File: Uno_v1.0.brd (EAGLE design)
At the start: 68.6 x 53.3 mm, 62 parts, among them CN1 POWER_JACK, CN2 47346-0001, CN3 DIGITAL10, CN4 DIGITAL8, CN5 ICSP, CN6 POWER8, CN7 ANALOG6, IC1 AMS1117-5.0, IC2 AMS1117-3.3, IC3 MCP6002T-I/SN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

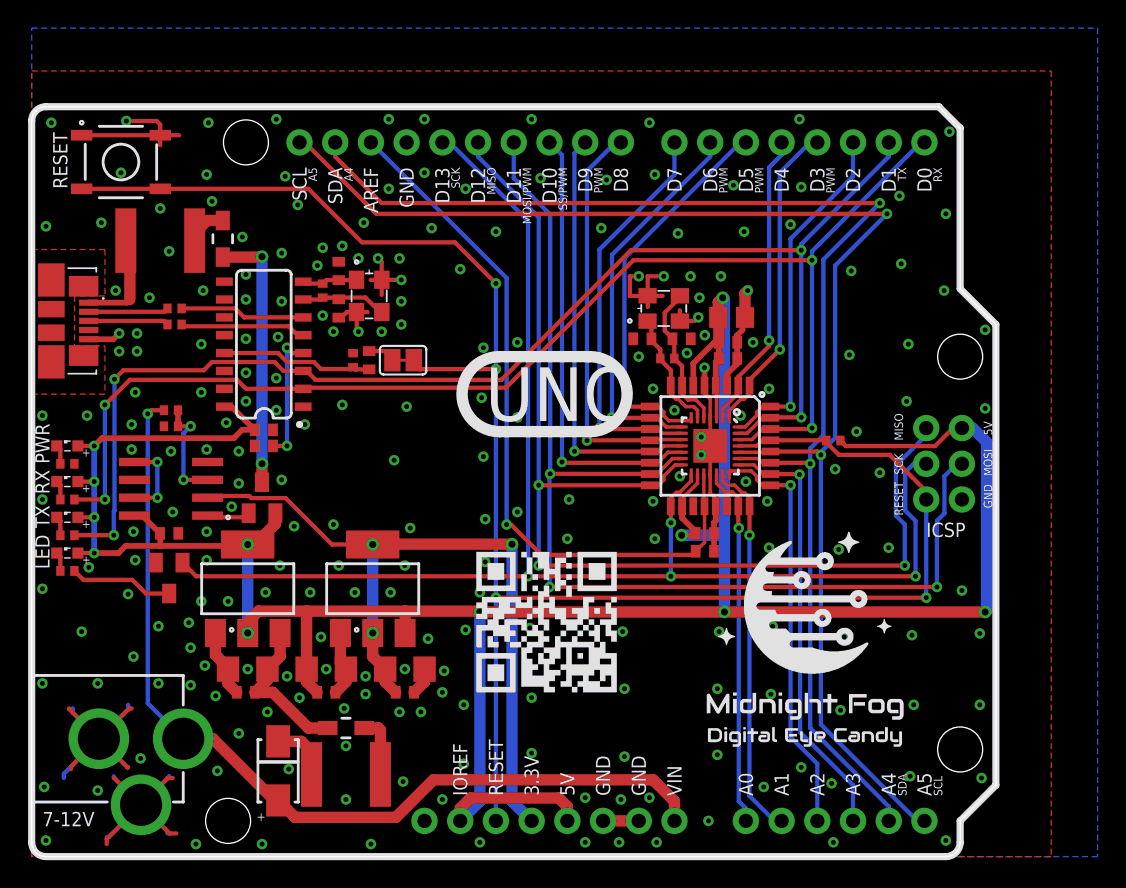
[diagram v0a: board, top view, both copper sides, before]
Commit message: Moved main MCU a little bit to the right. Generated new CAM. Generated new preview.
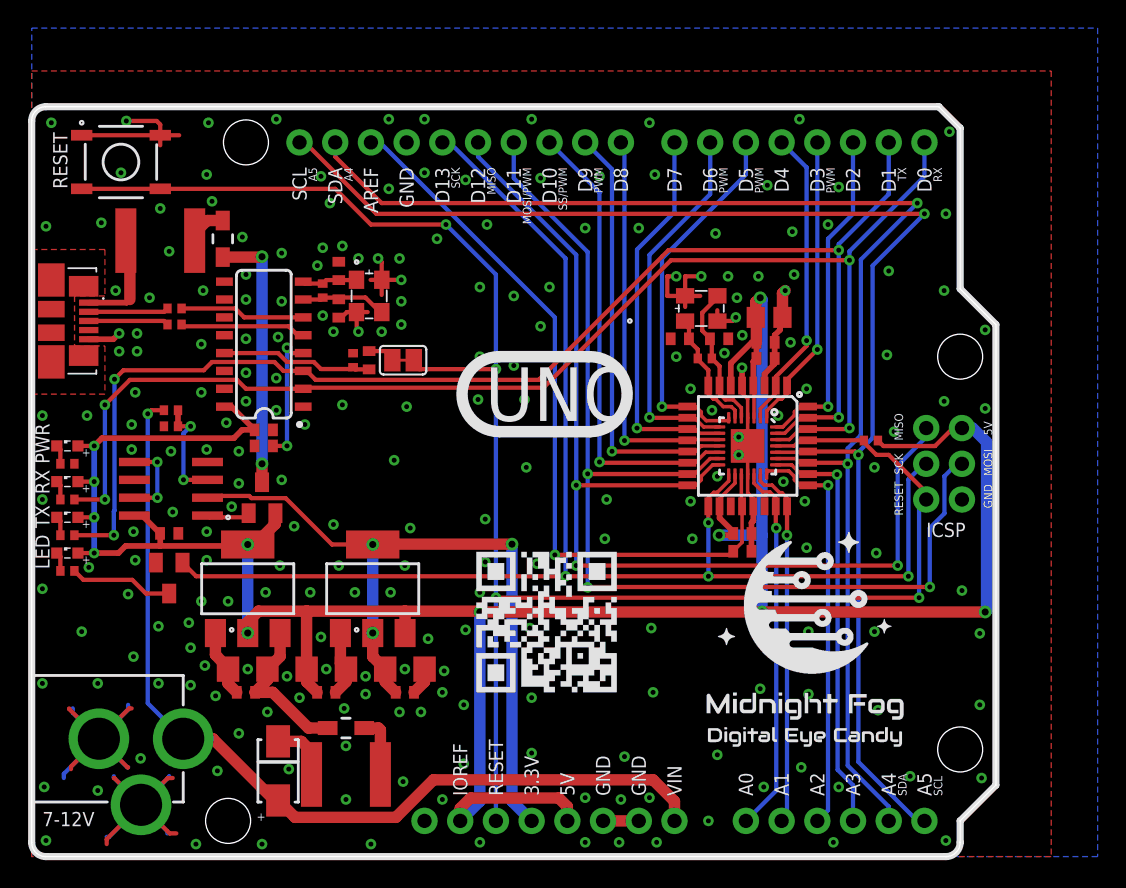
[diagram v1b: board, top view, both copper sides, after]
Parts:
- moved C12 2.67 mm to (48.9, 36.8)
- moved C13 2.67 mm to (46.1, 36.8)
- moved C14 2.67 mm to (52.2, 36.6)
- moved C15 2.67 mm to (52.2, 35.4)
- moved C16 2.67 mm to (50.5, 23.0)
- moved C17 2.67 mm to (52.5, 38.4)
- moved C19 2.67 mm to (50.5, 21.7)
- moved Q2 2.67 mm to (47.6, 39.0)
- moved U2 2.67 mm to (50.9, 29.2)
- moved U3 2.67 mm to (50.9, 29.2)
- moved R12 2.67 mm to (59.7, 29.6)
- moved R6 2.67 mm to (47.9, 35.4)
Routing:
- net 5V: track 205.8 -> 203.1 mm
- net RESET: track 131.1 -> 128.4 mm
- net D12_MISO: track 79.8 -> 77.4 mm
- net AREF: track 51.4 -> 53.7 mm
- net D11_MOSI: track 79.8 -> 78.0 mm
- net D1_TX: track 94.7 -> 96.3 mm
- net A5_SCL: track 98.4 -> 99.9 mm
- net A4_SDA: track 94.7 -> 96.3 mm
- net D0_RX: track 93.3 -> 94.8 mm
- net D3_PWM: track 22.6 -> 21.2 mm
- net D5_PWM: track 28.1 -> 26.8 mm
- net D8: track 29.2 -> 28.1 mm
- net D2: track 25.1 -> 24.0 mm
- net A3: track 30.8 -> 29.7 mm
- net D6_PWM: track 27.7 -> 26.6 mm
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
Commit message: Moved some wires. Generated new CAM. Generated new preview.
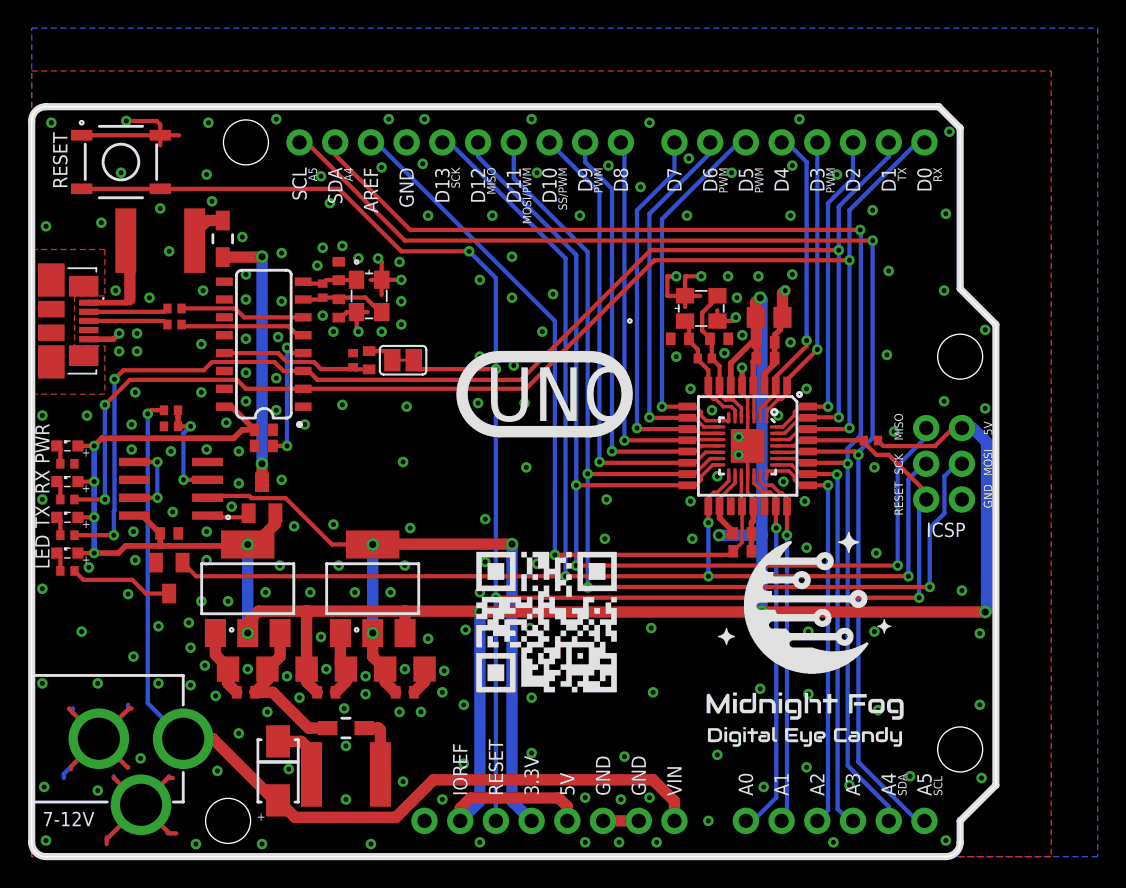
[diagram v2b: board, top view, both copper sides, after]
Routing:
- net A4_SDA: track 96.3 -> 89.4 mm
- net A5_SCL: track 99.9 -> 93.6 mm
- net GND: vias 228 -> 229

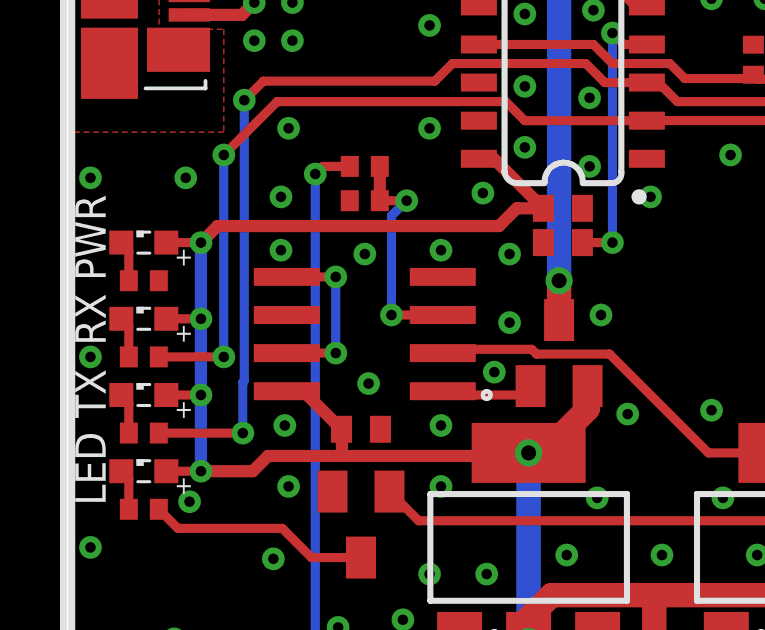
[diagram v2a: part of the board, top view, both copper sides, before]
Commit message: Use LM358D OpAmp instead. Generated new CAM. Generated new PNG preview. Generated new PDF schematic.
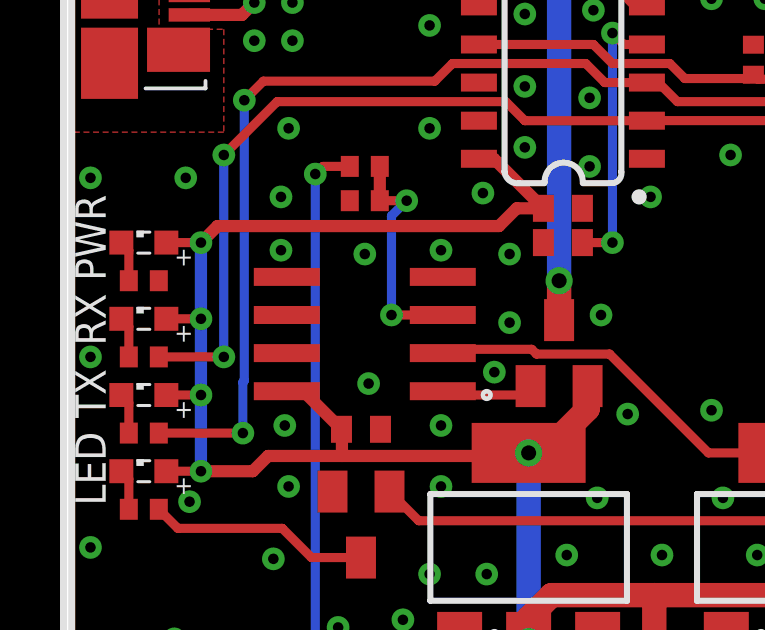
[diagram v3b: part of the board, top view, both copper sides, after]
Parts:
- IC3: value MCP6002T-I/SN -> LM358D
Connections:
- removed net N$1: IC3.5, IC3.7
- net GND: now also IC3.5
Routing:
- net N$1: track 5.81 -> 0.00 mm, vias 2 -> 0
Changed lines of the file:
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@@
 <drawing>
 <settings>
-<setting alwaysvectorfont="yes"/>
+<setting alwaysvectorfont="no"/>
 <setting verticaltext="up"/>
 </settings>
@@
 <attribute name="VALUE" x="22.733" y="42.291" size="0.6096" layer="27" font="vector"/>
 </element>
-<element name="IC3" library="linear" library_urn="urn:adsk.eagle:library:262" package="SO08" package3d_urn="urn:adsk.eagle:package:16404/2" value="MCP6002T-I/SN" x="9.906" y="26.162" smashed="yes" rot="R90">
+<element name="IC3" library="linear" library_urn="urn:adsk.eagle:library:262" package="SO08" package3d_urn="urn:adsk.eagle:package:16404/2" value="LM358D" x="9.906" y="26.162" smashed="yes" rot="R90">
 <attribute name="NAME" x="8.509" y="27.559" size="0.6096" layer="27" font="vector"/>
 <attribute name="POPULARITY" value="4" x="9.906" y="26.162" size="1.778" layer="27" rot="R90" display="off"/>
@@
 <via x="38.989" y="45.593" extent="1-16" drill="0.35"/>
 <via x="35.941" y="48.641" extent="1-16" drill="0.35"/>
+<contactref element="IC3" pad="5"/>
 </signal>
 <signal name="VIN" class="3">
@@
 <wire x1="11.303" y1="30.607" x2="10.406" y2="30.607" width="0.3048" layer="1"/>
 </signal>
-<signal name="N$1">
-<contactref element="IC3" pad="5"/>
-<contactref element="IC3" pad="7"/>
-<wire x1="7.306" y1="25.527" x2="8.9408" y2="25.527" width="0.3048" layer="1"/>
-<via x="8.9408" y="25.527" extent="1-16" drill="0.35"/>
-<via x="8.938" y="28.067" extent="1-16" drill="0.35"/>
-<wire x1="8.938" y1="28.067" x2="8.938" y2="25.5298" width="0.3048" layer="16"/>
-<wire x1="8.9408" y1="25.527" x2="8.938" y2="25.5298" width="0.3048" layer="16"/>
-<wire x1="8.938" y1="28.067" x2="7.306" y2="28.067" width="0.3048" layer="1"/>
-</signal>
 <signal name="MCU_OSC_IN">

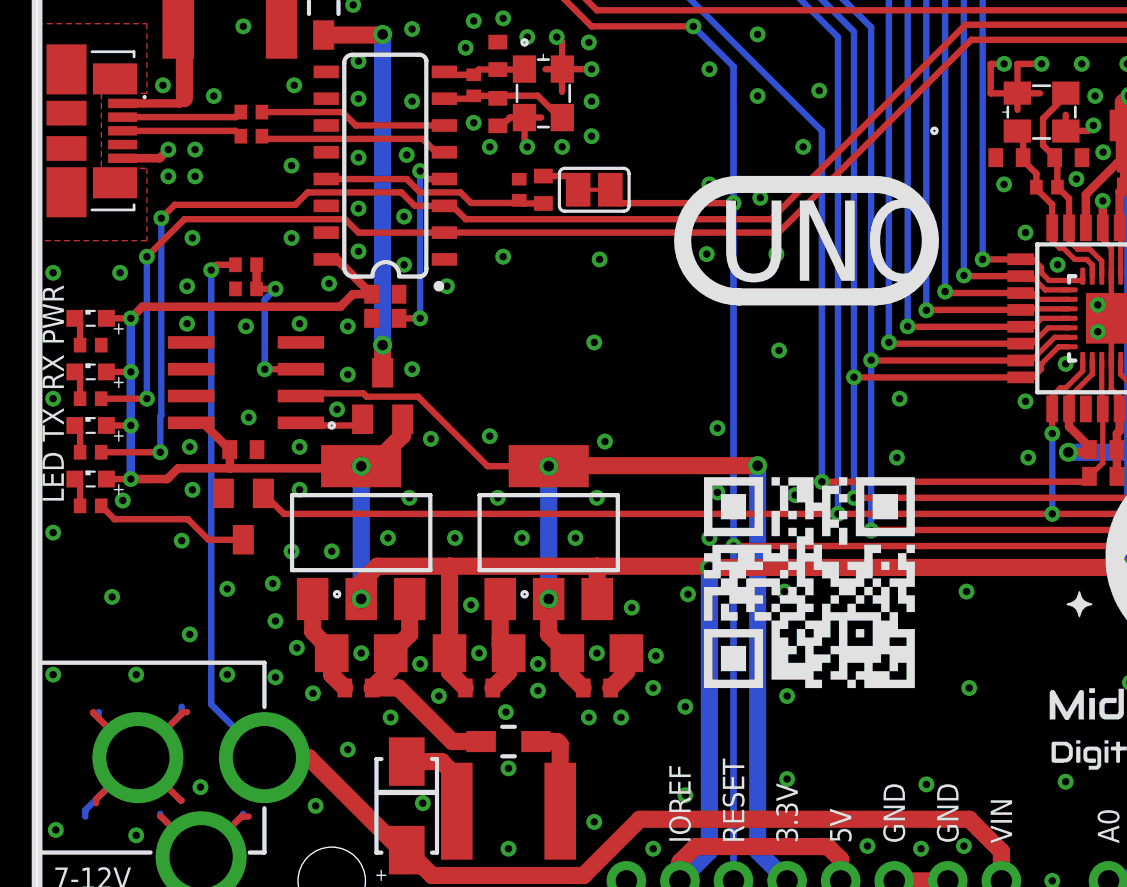
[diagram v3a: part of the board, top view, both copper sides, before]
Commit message: Properly disabled second channel of op amp. Generated new CAM files. Generated new PNG preview. Generated new PDF schematics. Generated new BoM and PnP files.
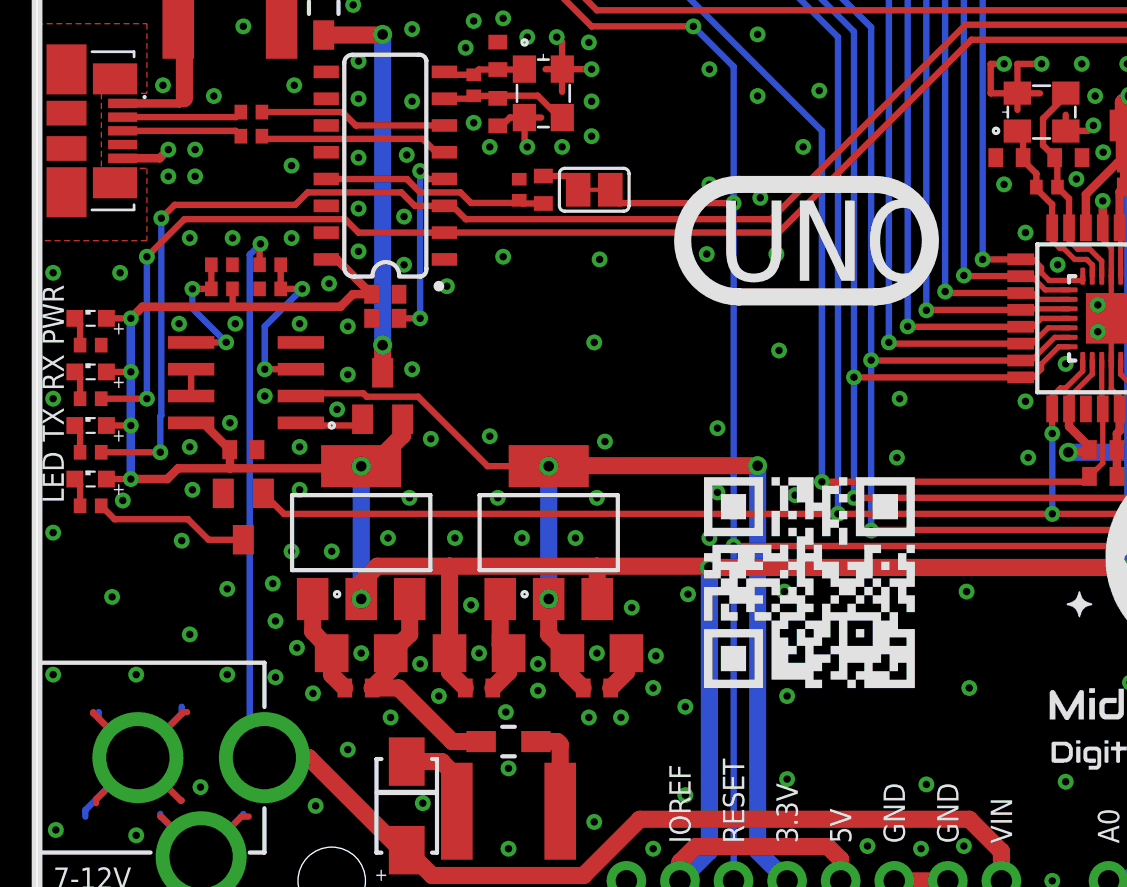
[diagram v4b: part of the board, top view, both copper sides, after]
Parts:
- added R13, R14: 100K, rcl:R0402
- moved R4 1.14 mm to (11.0, 31.8)
- moved R5 1.14 mm to (11.0, 30.6)
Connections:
- new net N$1: IC3.5, R13.1, R14.2
- new net N$15: IC3.6, IC3.7
- net 5V: now also R13.2
- net GND: now also R14.1; no longer IC3.5, IC3.6
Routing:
- net N$1: track 0.00 -> 6.90 mm, vias 0 -> 2
- net N$15: track 0.00 -> 1.27 mm
- net 5V: track 203.1 -> 204.0 mm
- net N$12: track 7.77 -> 8.42 mm
- net GND: vias 229 -> 230

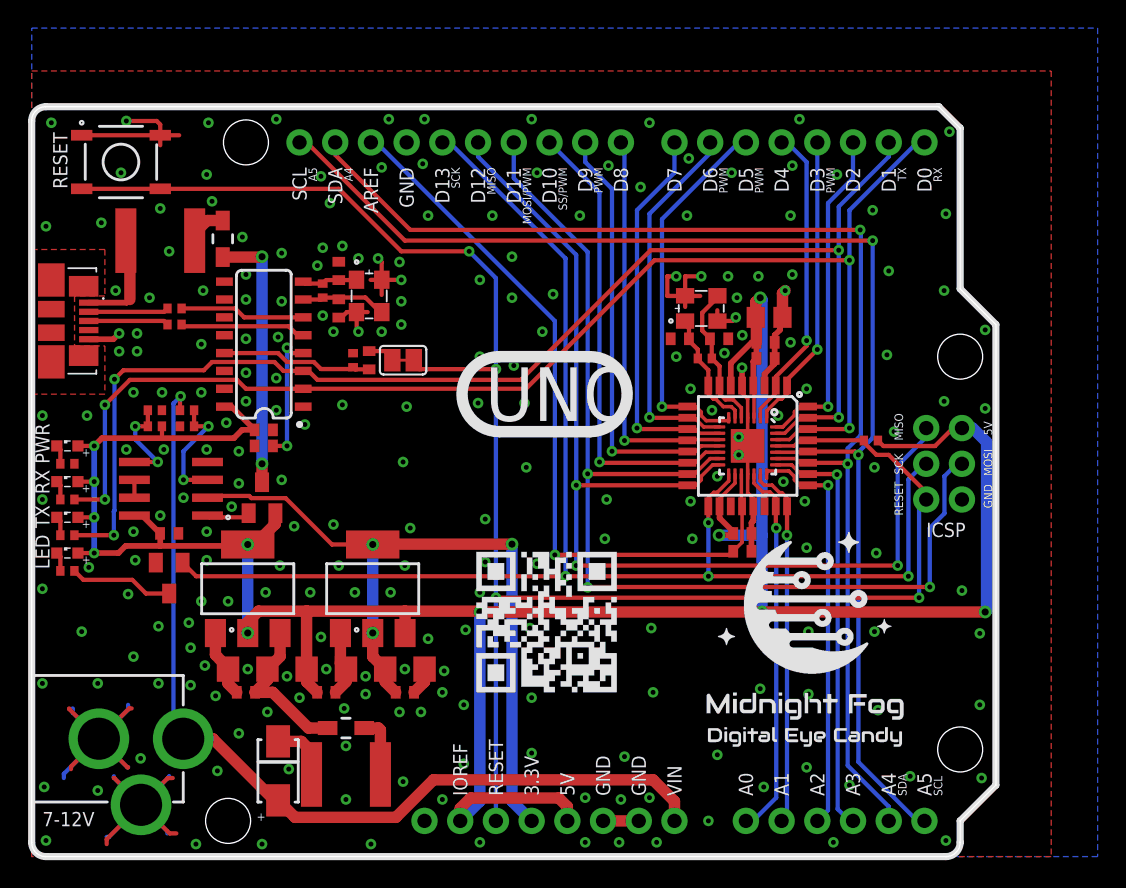
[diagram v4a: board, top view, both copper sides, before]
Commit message: Redone chip wiring for better reverse currents.
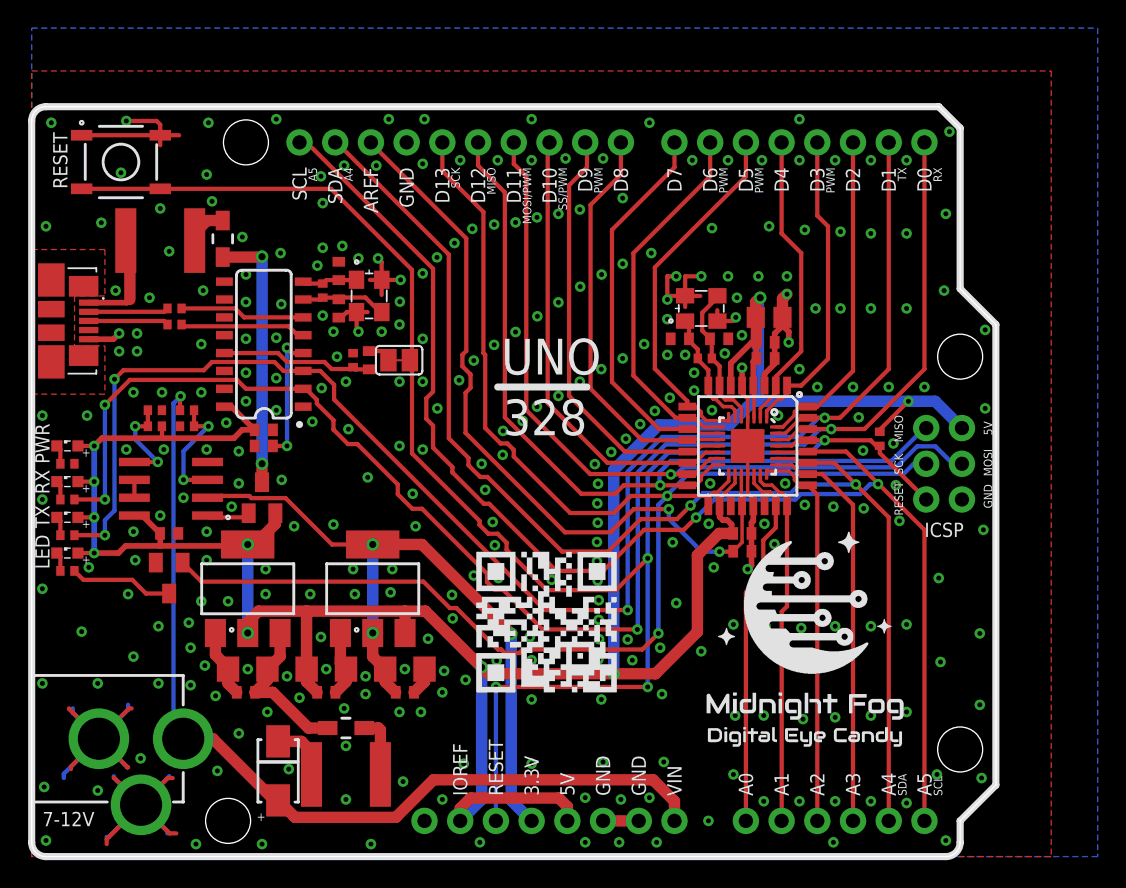
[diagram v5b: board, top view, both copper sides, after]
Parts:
- moved R12 0.65 mm to (60.3, 29.7), turned to 90 degrees
- moved SJ1 0.28 mm to (26.1, 35.3)
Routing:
- net D11_MOSI: track 77.9 -> 57.6 mm, vias 3 -> 1
- net D12_MISO: track 77.4 -> 60.1 mm, vias 3 -> 1
- net D0_RX: track 95.0 -> 111.2 mm
- net D1_TX: track 96.3 -> 110.0 mm
- net D13_SCK: track 103.5 -> 111.1 mm, vias 4 -> 2
- net 5V: track 204.0 -> 196.7 mm, vias 11 -> 10
- net 3.3V: track 55.4 -> 50.8 mm
- net A5_SCL: track 93.6 -> 98.1 mm
- net RESET: track 128.3 -> 124.4 mm
- net GND: track 115.2 -> 118.3 mm, vias 230 -> 313
- net A2: track 29.3 -> 27.8 mm, vias 1 -> 0
- net D3_PWM: track 21.2 -> 22.4 mm, vias 1 -> 0
- net D8: track 28.1 -> 29.1 mm, vias 1 -> 0
- net A4_SDA: track 89.4 -> 90.4 mm
- net D5_PWM: track 27.1 -> 26.2 mm, vias 1 -> 0
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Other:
- board text added: "328"
- board text added: "UNO/328 v1.0 (c) Andriy Golovnya Designed in Germany http://redscorp.net"
- board text removed: "UNO v1.0 (c) Andriy Golovnya Designed in Germany http://redscorp.net"
